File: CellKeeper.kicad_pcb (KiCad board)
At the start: 4 copper layers, 306 x 113 mm, 506 parts, among them J1 Screw_Terminal_01x04, J10 3.81P Screw Terminal, J11 USB_C_Receptacle_USB2.0_16P, J12 Conn_02x10_Odd_Even, J14 OEM Shunt Connector, J15 Screw_Terminal_01x04, J16 Conn_01x03, J17 OEM HV Sense Connector, J18 7.62mm Pitch Screw Terminal, J19 USB_C_Receptacle_USB2.0_16P, J2 Screw_Terminal_01x01, J20 OEM Connector, J21 3.81P Screw Terminal, J22 Conn_02x10_Odd_Even, J23 OEM Connector, J24 3.81P Screw Terminal, J3 Screw_Terminal_01x04, J4 8P8C_LED_Shielded_x2, J5 8P8C_LED_Shielded_x2, J6 OEM Connector, J7 Screw_Terminal_01x04, J8 Conn_01x03, J9 USB_C_Receptacle_USB2.0_16P, Q1 BSC0805LS, Q2 BSC0805LS, Q3 BSC0805LS, Q4 BSC0805LS, SW1 TS-1187A-B-A-B, SW2 TS-1187A-B-A-B, SW3 TS-1187A-B-A-B, SW4 TS-1187A-B-A-B, U1 UCC27524DR, U10 ISO1050DUB, U11 UCC27524DR, U12 LTV-217-B-G, U13 LTV-217-B-G, U14 RP2354B, U15 F0505S-1WR3, U16 ISO1540, U17 INA228, U18 ADS1115, U19 ADS1115, U20 RP2354B, U21 SP3485EN-L/TR, U22 AM26LV32EIDR, U23 SP3485EN-L/TR, U24 AM26LV32EIDR, U25 TLV1117LV33DCYR, U26 TLV1117LV33DCYR, U3 TPS5430DDAR, U4 F0505S-1WR3, U5 ISO1050DUB, U6 LTV-217-B-G, U7 LTV-217-B-G, U8 LTV-217-B-G, U9 LTV-217-B-G, Y1 ABM8-272-T3, Y2 ABM8-272-T3

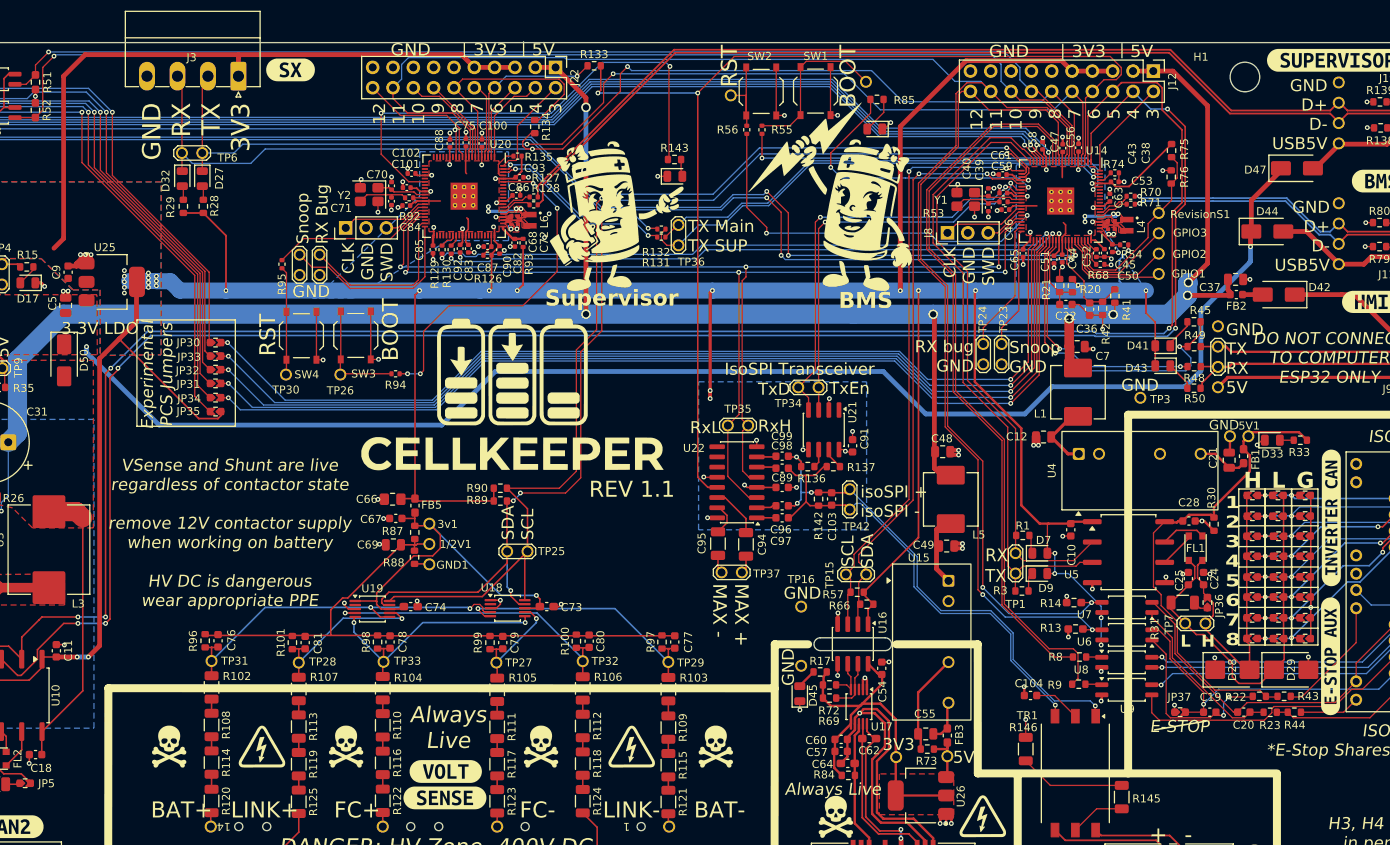
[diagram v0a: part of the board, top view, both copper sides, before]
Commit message: Rev1.1: USB VBUS sense on GPIO3, revision strap, shunt 3V3 cap
- USB VBUS detect for both MCUs: 3.3k from each connector's VBUS to GPIO3
  (pin 80) and 5.1k to GND (controller R78/R153, Supervisor R155/R154), also
  brought out on J12/J22 pin 2.
- Revision strap on GPIO47: R75 10k to 3V3, R76 1k to GND (reads as Rev1.1).
- C116 10uF on the isolated shunt 3V3; C57 removed.
- Test points: GPIO1-3 removed, GPIO44-46 added.
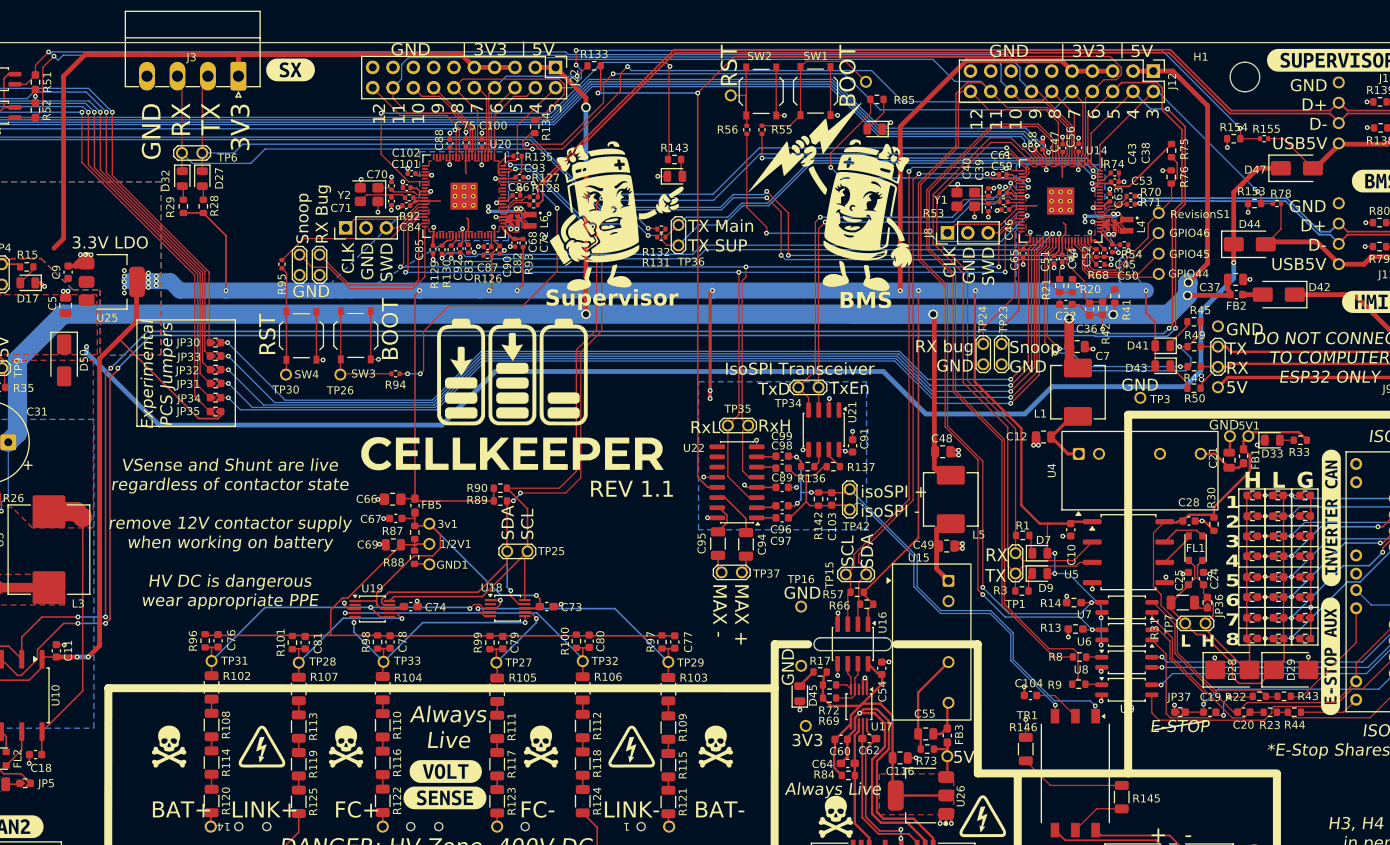
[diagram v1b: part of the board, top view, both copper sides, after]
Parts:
- removed C57: 1uF, CellKeeper_Local:Capacitor_SMD__C_0603_1608Metric
- removed GPIO3: TP, CellKeeper_Local:BMS_Library__TestPoint_THTPad_D1.5mm_Drill1.0mm
- added C116: 10uF, CellKeeper_Local:Capacitor_SMD__C_0805_2012Metric, F.Cu at (238.7, 131.8)
- added GPIO46: TP, CellKeeper_Local:BMS_Library__TestPoint_THTPad_D1.5mm_Drill1.0mm, F.Cu at (271.0, 66.2)
- added R153: 5.1k, CellKeeper_Local:Resistor_SMD__R_0603_1608Metric, F.Cu at (283.0, 62.5)
- added R154: 5.1k, CellKeeper_Local:Resistor_SMD__R_0603_1608Metric, F.Cu at (280.4, 54.4)
- added R155: 3.3k, CellKeeper_Local:Resistor_SMD__R_0402_1005Metric, F.Cu at (284.2, 54.4)
- added R78: 3.3k, CellKeeper_Local:Resistor_SMD__R_0402_1005Metric, F.Cu at (285.8, 62.5)
- R75: value 47k -> 10k
- R76: value 0r -> 1k
- moved TP49 12.0 mm to (226.9, 127.8)
- moved D44 2.72 mm to (282.4, 67.6)
- renumbered GPIO1 to GPIO44, GPIO2 to GPIO45
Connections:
- net /GPIO3 renamed VBUS Detect USB1
- net /MCU2_GPIO3 renamed VBUS Detect USB2
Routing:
- net VBUS Detect USB2: track 13.0 -> 111.2 mm, vias 0 -> 3
- net VBUS Detect USB1: track 12.7 -> 34.0 mm, vias 0 -> 1
- net Net-(D44-A): track 24.7 -> 32.4 mm
- net Net-(D47-A): track 20.6 -> 27.7 mm
- net GND: track 247.6 -> 249.8 mm, vias 156 -> 158
- net +LDO_IN: track 180.4 -> 182.1 mm
- net GND Shunt NTC -: track 82.5 -> 83.6 mm, vias 8 -> 9
